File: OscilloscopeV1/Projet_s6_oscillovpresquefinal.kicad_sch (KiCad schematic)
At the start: 34 parts, among them IC1 PGA849RGTR, J1 Conn_Coaxial, J2 Conn_01x06_Socket, J3 PILES_3AA, J4 Conn_01x05_Pin, SW1 SW_SPST, U1 MCP6001-OT, U2 AP2112K-3.3, U3 MCP1640x-xCHY, U4 STM32L476RGTx

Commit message: Ajout du schématique final
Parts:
- C1, C10, C11, C12, C2, C3, C4, C5, C6, C7, C8, C9: footprint (none) -> Capacitor_SMD:C_0805_2012Metric_Pad1.18x1.45mm_HandSolder
- H1, H2, H3, H4: footprint (none) -> MountingHole:MountingHole_3.2mm_M3_DIN965_Pad
- J1: footprint (none) -> Connector_PinHeader_2.54mm:PinHeader_1x06_P2.54mm_Vertical
- J3: footprint (none) -> Connector_PinHeader_2.54mm:PinHeader_1x02_P2.54mm_Vertical
- J4: footprint (none) -> Connector_PinHeader_2.54mm:PinHeader_1x05_P2.54mm_Vertical
- L1: footprint (none) -> Inductor_SMD:L_0805_2012Metric_Pad1.05x1.20mm_HandSolder
- R1, R2, R3, R4, R5: footprint (none) -> Resistor_SMD:R_0805_2012Metric_Pad1.20x1.40mm_HandSolder
- SW1: footprint (none) -> Button_Switch_THT:SW_Slide_SPDT_Straight_CK_OS102011MS2Q
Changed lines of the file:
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@@
 			)
 		)
-		(property "Footprint" ""
+		(property "Footprint" "Capacitor_SMD:C_0805_2012Metric_Pad1.18x1.45mm_HandSolder"
 			(at 196.5452 242.57 0)
 			(effects
@@
 			)
 		)
-		(property "Footprint" ""
+		(property "Footprint" "Connector_PinHeader_2.54mm:PinHeader_1x02_P2.54mm_Vertical"
 			(at 241.3 205.74 0)
 			(effects
@@
 			)
 		)
-		(property "Footprint" ""
+		(property "Footprint" "Capacitor_SMD:C_0805_2012Metric_Pad1.18x1.45mm_HandSolder"
 			(at 347.98 66.04 0)
 			(effects
@@
 			)
 		)
-		(property "Footprint" ""
+		(property "Footprint" "Capacitor_SMD:C_0805_2012Metric_Pad1.18x1.45mm_HandSolder"
 			(at 77.47 191.77 0)
 			(effects
@@
 			)
 		)
-		(property "Footprint" ""
+		(property "Footprint" "Resistor_SMD:R_0805_2012Metric_Pad1.20x1.40mm_HandSolder"
 			(at 124.46 58.42 0)
 			(effects
@@
 			)
 		)
-		(property "Footprint" ""
+		(property "Footprint" "MountingHole:MountingHole_3.2mm_M3_DIN965_Pad"
 			(at 299.72 213.36 0)
 			(effects
@@
 			)
 		)
-		(property "Footprint" ""
+		(property "Footprint" "Capacitor_SMD:C_0805_2012Metric_Pad1.18x1.45mm_HandSolder"
 			(at 359.41 67.31 0)
 			(effects
@@
 			)
 		)
-		(property "Footprint" ""
+		(property "Footprint" "Capacitor_SMD:C_0805_2012Metric_Pad1.18x1.45mm_HandSolder"
 			(at 361.95 74.93 0)
 			(effects
@@
 			)
 		)
-		(property "Footprint" ""
+		(property "Footprint" "Resistor_SMD:R_0805_2012Metric_Pad1.20x1.40mm_HandSolder"
 			(at 54.61 241.3 0)
 			(effects
@@
 			)
 		)
-		(property "Footprint" ""
+		(property "Footprint" "Capacitor_SMD:C_0805_2012Metric_Pad1.18x1.45mm_HandSolder"
 			(at 336.55 74.93 0)
 			(effects
@@
 			)
 		)
-		(property "Footprint" ""
+		(property "Footprint" "Inductor_SMD:L_0805_2012Metric_Pad1.05x1.20mm_HandSolder"
 			(at 229.87 233.68 0)
 			(effects
@@
 			)
 		)
-		(property "Footprint" ""
+		(property "Footprint" "Capacitor_SMD:C_0805_2012Metric_Pad1.18x1.45mm_HandSolder"
 			(at 80.01 187.96 0)
 			(effects
@@
 			)
 		)
-		(property "Footprint" ""
+		(property "Footprint" "Connector_PinHeader_2.54mm:PinHeader_1x06_P2.54mm_Vertical"
 			(at 39.37 160.02 0)
 			(effects
@@
 			)
 		)
-		(property "Footprint" ""
+		(property "Footprint" "MountingHole:MountingHole_3.2mm_M3_DIN965_Pad"
 			(at 299.72 229.87 0)
 			(effects
@@
 			)
 		)
-		(property "Footprint" ""
+		(property "Footprint" "Capacitor_SMD:C_0805_2012Metric_Pad1.18x1.45mm_HandSolder"
 			(at 353.06 66.04 0)
 			(effects
@@
 			)
 		)
-		(property "Footprint" ""
+		(property "Footprint" "MountingHole:MountingHole_3.2mm_M3_DIN965_Pad"
 			(at 299.72 219.71 0)
 			(effects
@@
 			)
 		)
-		(property "Footprint" ""
+		(property "Footprint" "Resistor_SMD:R_0805_2012Metric_Pad1.20x1.40mm_HandSolder"
 			(at 245.11 245.618 90)
 			(effects
@@
 			)
 		)
-		(property "Footprint" ""
+		(property "Footprint" "MountingHole:MountingHole_3.2mm_M3_DIN965_Pad"
 			(at 299.72 224.79 0)
 			(effects
@@
 			)
 		)
-		(property "Footprint" ""
+		(property "Footprint" "Resistor_SMD:R_0805_2012Metric_Pad1.20x1.40mm_HandSolder"
 			(at 124.46 46.99 0)
 			(effects
@@
 			)
 		)
-		(property "Footprint" ""
+		(property "Footprint" "Resistor_SMD:R_0805_2012Metric_Pad1.20x1.40mm_HandSolder"
 			(at 245.11 249.428 90)
 			(effects
@@
 			)
 		)
-		(property "Footprint" ""
+		(property "Footprint" "Capacitor_SMD:C_0805_2012Metric_Pad1.18x1.45mm_HandSolder"
 			(at 323.85 83.82 0)
 			(effects
@@
 			)
 		)
-		(property "Footprint" ""
+		(property "Footprint" "Capacitor_SMD:C_0805_2012Metric_Pad1.18x1.45mm_HandSolder"
 			(at 341.63 67.31 0)
 			(effects
@@
 			)
 		)
-		(property "Footprint" ""
+		(property "Footprint" "Capacitor_SMD:C_0805_2012Metric_Pad1.18x1.45mm_HandSolder"
 			(at 240.03 231.14 0)
 			(effects
@@
 			)
 		)
-		(property "Footprint" ""
+		(property "Footprint" "Button_Switch_THT:SW_Slide_SPDT_Straight_CK_OS102011MS2Q"
 			(at 201.93 196.85 0)
 			(effects
@@
 			)
 		)
-		(property "Footprint" ""
+		(property "Footprint" "Connector_PinHeader_2.54mm:PinHeader_1x05_P2.54mm_Vertical"
 			(at 341.63 208.28 0)
 			(effects
@@
 			)
 		)
-		(property "Footprint" ""
+		(property "Footprint" "Capacitor_SMD:C_0805_2012Metric_Pad1.18x1.45mm_HandSolder"
 			(at 80.01 132.08 0)
 			(effects

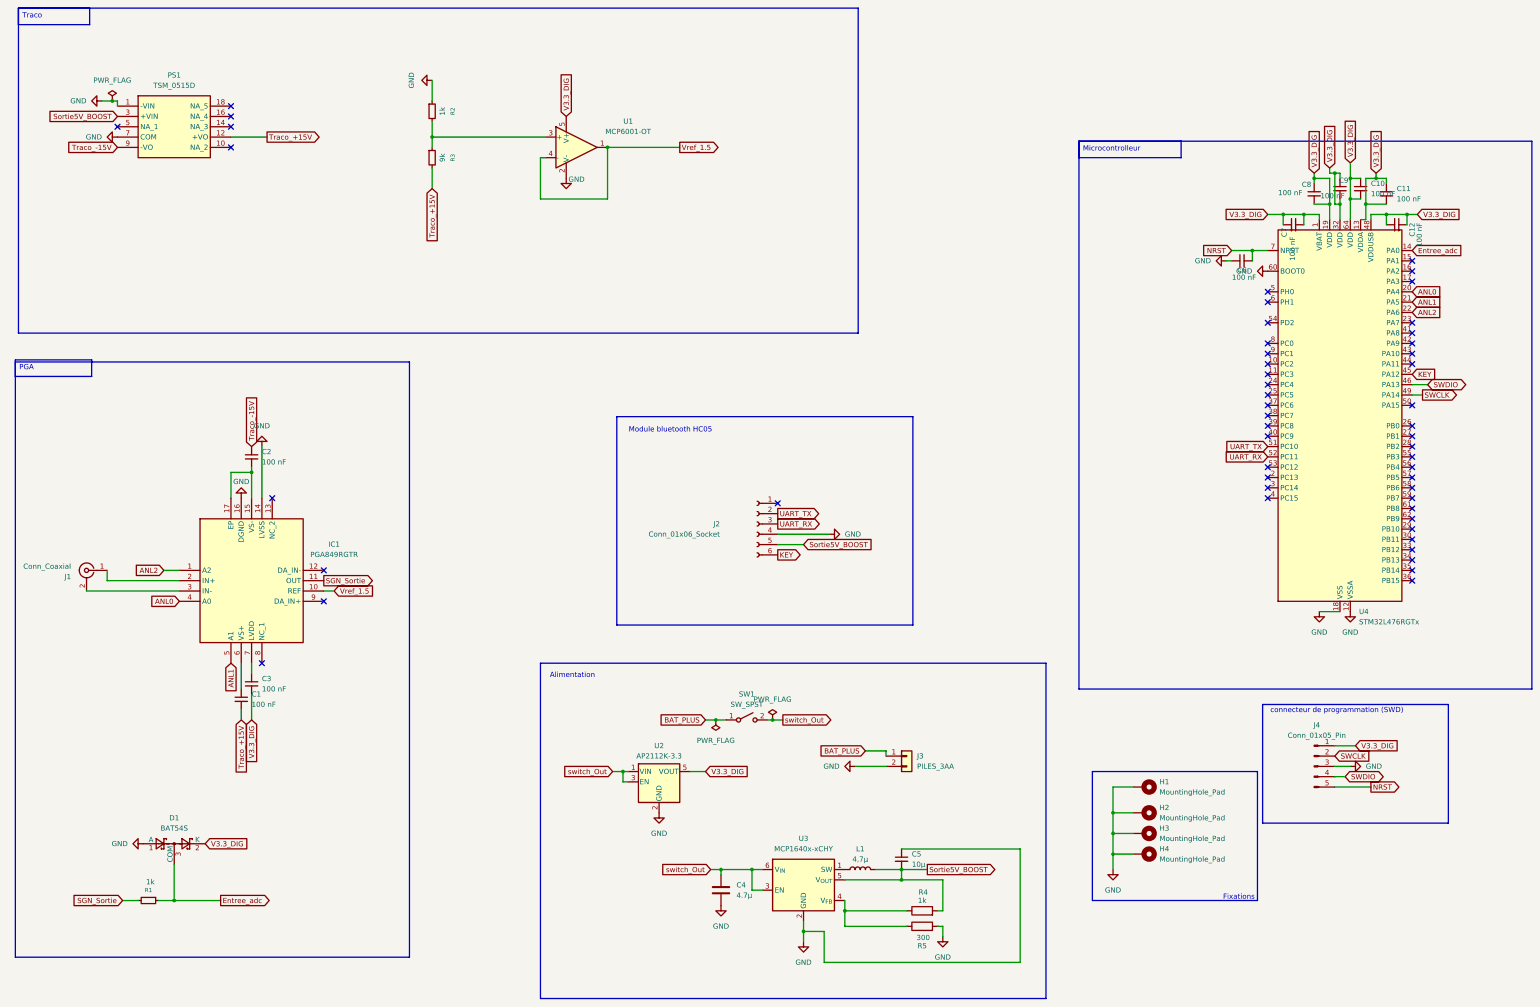
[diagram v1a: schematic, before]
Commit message: Modification du système d'alimentation / tension de 1,5V
Modification du système d'alimentation et remplacement du suiveur par une diode zener
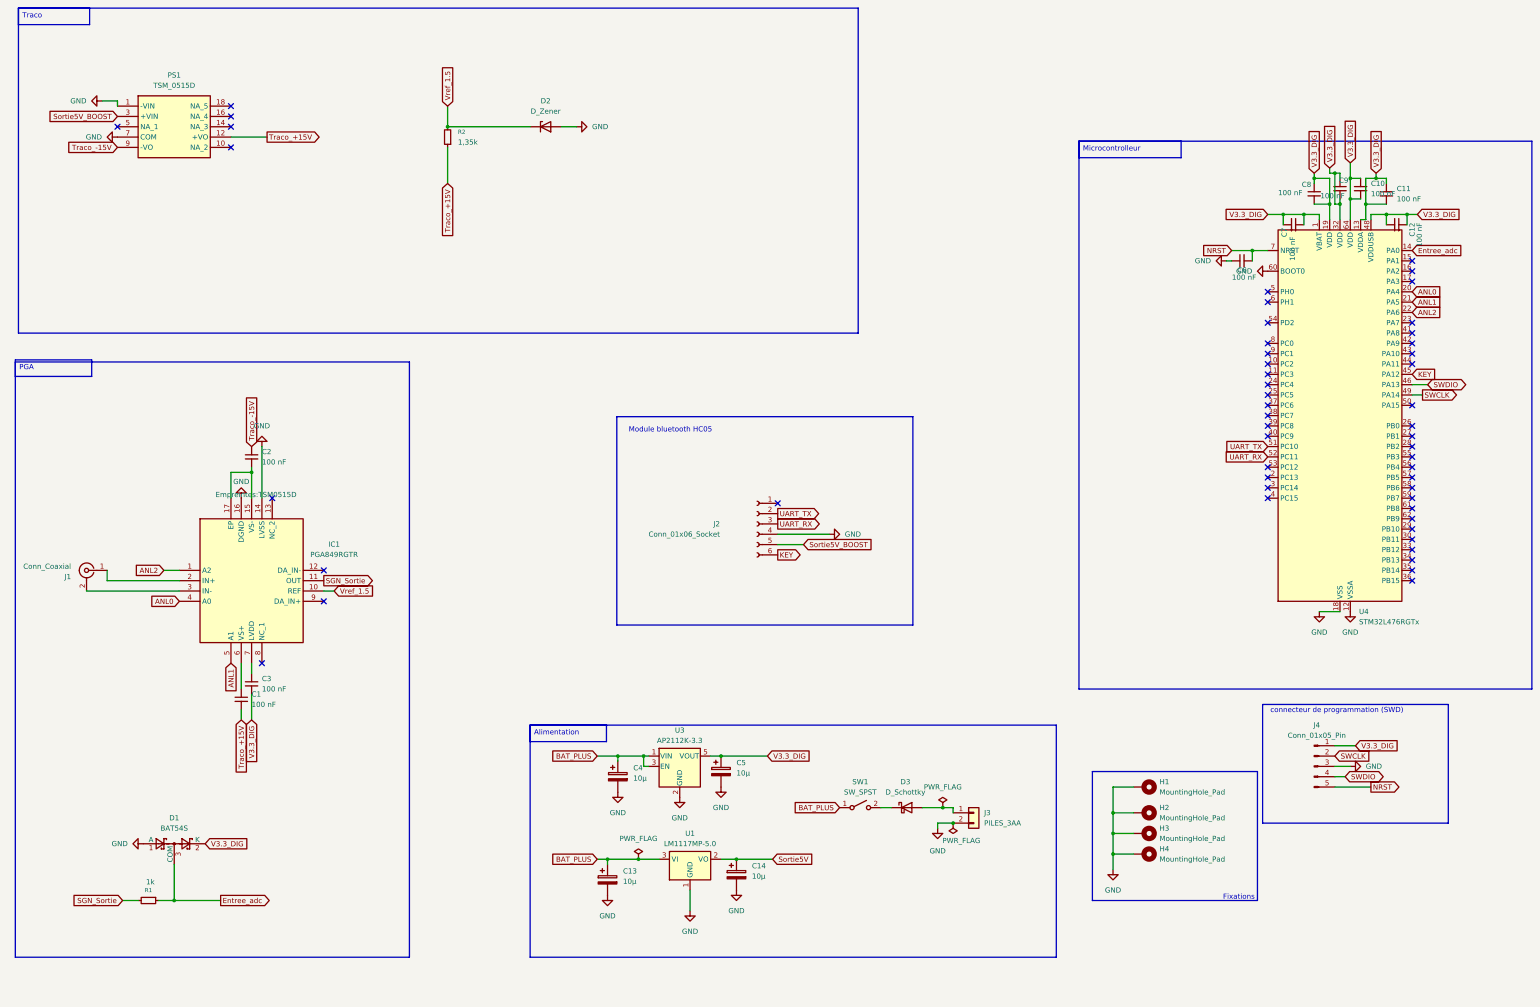
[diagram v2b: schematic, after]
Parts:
- removed C4: 4.7µ, Capacitor_SMD:C_0805_2012Metric_Pad1.18x1.45mm_HandSolder, symbol Device:C
- removed C5: 10µ, Capacitor_SMD:C_0805_2012Metric_Pad1.18x1.45mm_HandSolder, symbol Device:C_Small
- removed L1: 4,7µ, Inductor_SMD:L_0805_2012Metric_Pad1.05x1.20mm_HandSolder, symbol Device:L
- removed R3: 9k, Resistor_SMD:R_0805_2012Metric_Pad1.20x1.40mm_HandSolder, symbol Device:R_Small
- removed R4: 1k, Resistor_SMD:R_0805_2012Metric_Pad1.20x1.40mm_HandSolder, symbol Device:R
- removed R5: 300, Resistor_SMD:R_0805_2012Metric_Pad1.20x1.40mm_HandSolder, symbol Device:R
- removed U1: MCP6001-OT, Package_TO_SOT_SMD:SOT-23-5, symbol Amplifier_Operational:MCP6001-OT
- removed U3: MCP1640x-xCHY, Package_TO_SOT_SMD:SOT-23-6, symbol Regulator_Switching:MCP1640x-xCHY
- added C13, C14: 10µ, symbol Device:C_Polarized
- added C4, C5: 10µ, Capacitor_SMD:C_0805_2012Metric_Pad1.18x1.45mm_HandSolder, symbol Device:C_Polarized
- added D2: D_Zener, symbol Device:D_Zener
- added D3: D_Schottky, symbol Device:D_Schottky
- added U1: LM1117MP-5.0, Package_TO_SOT_SMD:SOT-223-3_TabPin2, symbol Regulator_Linear:LM1117MP-5.0
- R2: value 1k -> 1,35k; footprint Resistor_SMD:R_0805_2012Metric_Pad1.20x1.40mm_HandSolder -> Resistor_SMD:R_0815_2038Metric_Pad1.20x4.05mm_HandSolder
- SW1: footprint Button_Switch_THT:SW_Slide_SPDT_Straight_CK_OS102011MS2Q -> Connector_PinHeader_2.54mm:PinHeader_1x05_P2.54mm_Vertical
- renumbered U2 to U3
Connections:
- net BAT_PLUS: now also U3.1 (VIN), U3.3 (EN), C13.1, C4.1, U1.3 (VI); no longer J3.1 (Pin_1)
- net GND: now also C13.2, C14.2, C4.2, C5.2, D2.2 (A), U1.1 (GND); no longer R2.1
- net Traco_+15V: now also R2.1
- net V3.3_DIG: now also C5.1
- net Vref_1.5: now also R2.2, D2.1 (K)
- removed net switch_Out: SW1.2 (B), U3.1 (VIN), U3.3 (EN)
- new net: D3.2 (A), J3.1 (Pin_1)
- new net: D3.1 (K), SW1.2 (B)
- new net Sortie5V: C14.1, U1.2 (VO)
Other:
- note removed: "Alimentation"
- moved on the sheet: J3, SW1, U3

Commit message: Ajout de toutes les empreintes
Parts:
- C13, C14: footprint (none) -> Capacitor_SMD:CP_Elec_5x5.4
- C4, C5: footprint Capacitor_SMD:C_0805_2012Metric_Pad1.18x1.45mm_HandSolder -> Capacitor_SMD:CP_Elec_5x5.4
- D2, D3: footprint (none) -> Diode_SMD:D_SOD-123
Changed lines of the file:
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@@
 			)
 		)
-		(property "Footprint" ""
+		(property "Footprint" "Capacitor_SMD:CP_Elec_5x5.4"
 			(at 168.6052 240.03 0)
 			(effects
@@
 			)
 		)
-		(property "Footprint" ""
+		(property "Footprint" "Diode_SMD:D_SOD-123"
 			(at 152.4 50.8 0)
 			(effects
@@
 			)
 		)
-		(property "Footprint" ""
+		(property "Footprint" "Capacitor_SMD:CP_Elec_5x5.4"
 			(at 200.3552 238.76 0)
 			(effects
@@
 			)
 		)
-		(property "Footprint" "Capacitor_SMD:C_0805_2012Metric_Pad1.18x1.45mm_HandSolder"
+		(property "Footprint" "Capacitor_SMD:CP_Elec_5x5.4"
 			(at 171.1452 214.63 0)
 			(effects
@@
 			)
 		)
-		(property "Footprint" ""
+		(property "Footprint" "Diode_SMD:D_SOD-123"
 			(at 241.3 218.44 0)
 			(effects
@@
 			)
 		)
-		(property "Footprint" "Capacitor_SMD:C_0805_2012Metric_Pad1.18x1.45mm_HandSolder"
+		(property "Footprint" "Capacitor_SMD:CP_Elec_5x5.4"
 			(at 196.5452 213.36 0)
 			(effects

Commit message: Finalisation Empreinte
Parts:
- C13, C14, C4, C5: footprint Capacitor_SMD:CP_Elec_5x5.4 -> Capacitor_SMD:CP_Elec_4x5.7
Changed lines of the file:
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@@
 			)
 		)
-		(property "Footprint" "Capacitor_SMD:CP_Elec_5x5.4"
+		(property "Footprint" "Capacitor_SMD:CP_Elec_4x5.7"
 			(at 168.6052 240.03 0)
 			(effects
@@
 			)
 		)
-		(property "Footprint" "Capacitor_SMD:CP_Elec_5x5.4"
+		(property "Footprint" "Capacitor_SMD:CP_Elec_4x5.7"
 			(at 200.3552 238.76 0)
 			(effects
@@
 			)
 		)
-		(property "Footprint" "Capacitor_SMD:CP_Elec_5x5.4"
+		(property "Footprint" "Capacitor_SMD:CP_Elec_4x5.7"
 			(at 171.1452 214.63 0)
 			(effects
@@
 			)
 		)
-		(property "Footprint" "Capacitor_SMD:CP_Elec_5x5.4"
+		(property "Footprint" "Capacitor_SMD:CP_Elec_4x5.7"
 			(at 196.5452 213.36 0)
 			(effects

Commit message: Avancement PCB
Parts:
- removed U1: LM1117MP-5.0, Package_TO_SOT_SMD:SOT-223-3_TabPin2, symbol Regulator_Linear:LM1117MP-5.0
- added U1: MCP1826S, Package_TO_SOT_SMD:SOT-223, symbol Regulator_Linear:MCP1826S
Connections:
- net BAT_PLUS: now also U1.1 (VI)
- net GND: now also U1.2 (GND)
- net Sortie5V: now also U1.3 (VO)
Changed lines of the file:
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@@
 	)
 	(junction
+		(at 199.39 231.14)
+		(diameter 0)
+		(color 0 0 0 0)
+	)
+	(junction
 		(at 292.1 224.79)
 		(diameter 0)
@@
 	)
 	(junction
+		(at 175.26 231.14)
+		(diameter 0)
+		(color 0 0 0 0)
+	)
+	(junction
 		(at 341.63 63.5)
 		(diameter 0)
@@
 	)
 	(junction
-		(at 175.26 231.14)
-		(diameter 0)
-		(color 0 0 0 0)
-	)
-	(junction
 		(at 167.64 231.14)
 		(diameter 0)
@@
 	)
 	(junction
-		(at 199.39 231.14)
-		(diameter 0)
-		(color 0 0 0 0)
-	)
-	(junction
 		(at 346.71 62.23)
 		(diameter 0)
@@
 	(wire
 		(pts
+			(xy 187.96 238.76) (xy 187.96 243.84)
+		)
+		(stroke
+			(width 0)
+			(type default)
+		)
+	)
+	(wire
+		(pts
 			(xy 74.93 135.89) (xy 80.01 135.89)
 		)
@@
 	(wire
 		(pts
+			(xy 175.26 231.14) (xy 180.34 231.14)
+		)
+		(stroke
+			(width 0)
+			(type default)
+		)
+	)
+	(wire
+		(pts
 			(xy 74.93 53.34) (xy 83.82 53.34)
 		)
@@
 	(wire
 		(pts
-			(xy 187.96 238.76) (xy 187.96 243.84)
-		)
-		(stroke
-			(width 0)
-			(type default)
-		)
-	)
-	(wire
-		(pts
 			(xy 292.1 229.87) (xy 292.1 233.68)
 		)
@@
 	(wire
 		(pts
-			(xy 199.39 231.14) (xy 195.58 231.14)
-		)
-		(stroke
-			(width 0)
-			(type default)
-		)
-	)
-	(wire
-		(pts
 			(xy 292.1 219.71) (xy 292.1 213.36)
 		)
@@
 	(wire
 		(pts
-			(xy 175.26 231.14) (xy 180.34 231.14)
-		)
-		(stroke
-			(width 0)
-			(type default)
-		)
-	)
-	(wire
-		(pts
 			(xy 60.96 241.3) (xy 72.39 241.3)
 		)
@@
 	(wire
 		(pts
+			(xy 195.58 231.14) (xy 199.39 231.14)
+		)
+		(stroke
+			(width 0)
+			(type default)
+		)
+	)
+	(wire
+		(pts
 			(xy 297.18 229.87) (xy 292.1 229.87)
 		)
@@
 	)
 	(symbol
+		(lib_id "Regulator_Linear:MCP1826S")
+		(at 187.96 231.14 0)
+		(unit 1)
+		(exclude_from_sim no)
+		(in_bom yes)
+		(on_board yes)
+		(dnp no)
+		(fields_autoplaced yes)
+		(property "Reference" "U1"
+			(at 187.96 224.79 0)
+			(effects
+				(font
+					(size 1.27 1.27)
+				)
+			)
+		)
+		(property "Value" "MCP1826S"
+			(at 187.96 227.33 0)
+			(effects
+				(font
+					(size 1.27 1.27)
+				)
+			)
+		)
+		(property "Footprint" "Package_TO_SOT_SMD:SOT-223"
+			(at 185.42 227.33 0)
+			(effects
+				(font
+					(size 1.27 1.27)
+				)
+				(hide yes)
+			)
+		)
+		(property "Datasheet" "http://ww1.microchip.com/downloads/en/DeviceDoc/22057B.pdf"
+			(at 187.96 224.79 0)
+			(effects
+				(font
+					(size 1.27 1.27)
+				)
+				(hide yes)
+			)
+		)
+		(property "Description" "1000mA, Low-Voltage, Low Quiescent Current LDO Regulator, SOT-223, TO-220, TO-263"
+			(at 187.96 231.14 0)
+			(effects
+				(font
+					(size 1.27 1.27)
+				)
+				(hide yes)
+			)
+		)
+		(pin "1"
+		)
+		(pin "2"
+		)
+		(pin "3"
+		)
+		(instances
+			(project ""
+				(path "/79a95597-2db4-4373-9cc6-70296586f172"
+					(reference "U1")
+					(unit 1)
+				)
+			)
+		)
+	)
+	(symbol
 		(lib_id "Device:C_Polarized")
 		(at 199.39 234.95 0)
@@
 					(unit 1)
 				)
-			)
-		)
-	)
-	(symbol
-		(lib_id "Regulator_Linear:LM1117MP-5.0")
-		(at 187.96 231.14 0)
-		(unit 1)
-		(exclude_from_sim no)
-		(in_bom yes)
-		(on_board yes)
-		(dnp no)
-		(fields_autoplaced yes)
-		(property "Reference" "U1"
-			(at 187.96 224.79 0)
-			(effects
-				(font
-					(size 1.27 1.27)
-				)
-			)
-		)
-		(property "Value" "LM1117MP-5.0"
-			(at 187.96 227.33 0)
-			(effects
-				(font
-					(size 1.27 1.27)
-				)
-			)
-		)
-		(property "Footprint" "Package_TO_SOT_SMD:SOT-223-3_TabPin2"
-			(at 187.96 231.14 0)
-			(effects
-				(font
-					(size 1.27 1.27)
-				)
-				(hide yes)
-			)
-		)
-		(property "Datasheet" "http://www.ti.com/lit/ds/symlink/lm1117.pdf"
-			(at 187.96 231.14 0)
-			(effects
-				(font
-					(size 1.27 1.27)
-				)
-				(hide yes)
-			)
-		)
-		(property "Description" "800mA Low-Dropout Linear Regulator, 5.0V fixed output, SOT-223"
-			(at 187.96 231.14 0)
-			(effects
-				(font
-					(size 1.27 1.27)
-				)
-				(hide yes)
-			)
-		)
-		(pin "3"
-		)
-		(pin "1"
-		)
-		(pin "2"
-		)
-		(instances
-			(project ""
-				(path "/79a95597-2db4-4373-9cc6-70296586f172"
-					(reference "U1")
-					(unit 1)
-				)

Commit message: Avancement PCB : Plans de masse et structuration
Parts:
- J1: footprint Connector_PinHeader_2.54mm:PinHeader_1x06_P2.54mm_Vertical -> Connector_Coaxial:BNC_TEConnectivity_1478204_Vertical
- J2: footprint Connector_Harwin:Harwin_M20-89006xx_1x06_P2.54mm_Horizontal -> Connector_PinSocket_2.54mm:PinSocket_1x06_P2.54mm_Horizontal
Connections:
- net Sortie5V_BOOST is gone; now on net Sortie5V: J2.5 (Pin_5), PS1.3 (+VIN)
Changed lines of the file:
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@@
 		)
 	)
-	(global_label "Sortie5V_BOOST"
+	(global_label "Sortie5V"
 		(shape input)
 		(at 215.9 153.67 0)
@@
 		)
 		(property "Intersheetrefs" "${INTERSHEET_REFS}"
-			(at 233.8228 153.67 0)
+			(at 226.7471 153.67 0)
 			(effects
 				(font
@@
 		)
 	)
-	(global_label "Sortie5V_BOOST"
+	(global_label "Sortie5V"
 		(shape input)
 		(at 46.99 48.26 180)
@@
 		)
 		(property "Intersheetrefs" "${INTERSHEET_REFS}"
-			(at 29.0672 48.26 0)
+			(at 36.1429 48.26 0)
 			(effects
 				(font
@@
 			)
 		)
-		(property "Footprint" "Connector_Harwin:Harwin_M20-89006xx_1x06_P2.54mm_Horizontal"
+		(property "Footprint" "Connector_PinSocket_2.54mm:PinSocket_1x06_P2.54mm_Horizontal"
 			(at 204.47 148.59 0)
 			(effects
@@
 		(on_board yes)
 		(dnp no)
-		(fields_autoplaced yes)
 		(property "Reference" "PS1"
 			(at 60.96 38.1 0)
@@
 		)
 		(property "Footprint" "Empreintes:TSM0515D"
-			(at 71.12 140.64 0)
+			(at 47.244 40.64 0)
 			(effects
 				(font
@@
 			)
 		)
-		(property "Footprint" "Connector_PinHeader_2.54mm:PinHeader_1x06_P2.54mm_Vertical"
+		(property "Footprint" "Connector_Coaxial:BNC_TEConnectivity_1478204_Vertical"
 			(at 39.37 160.02 0)
 			(effects
